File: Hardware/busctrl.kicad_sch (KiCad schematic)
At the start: 22 parts, among them J13 ICSP, J2 Conn_02x05_Odd_Even, J8 POWER, J8 RESET, J9 IDE, SW1 PWR, SW1 RST, U2 ATF1508AS, U3 CY23022, U30 ATmega328P-P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

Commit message: PCB cleanup
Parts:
- added C15: 1uF, Capacitor_SMD:C_0402_1005Metric_Pad0.74x0.62mm_HandSolder, symbol Device:C_Small
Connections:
- net +5V: no longer C28.1, C28.1, J13.2 (Pin_2), R6.1, U30.20 (AVCC), U30.7 (VCC)
- net GND: now also C15.2
- new net +5VP: C15.1, C28.1, C28.1, J13.2 (Pin_2), R6.1, U30.20 (AVCC), U30.7 (VCC)

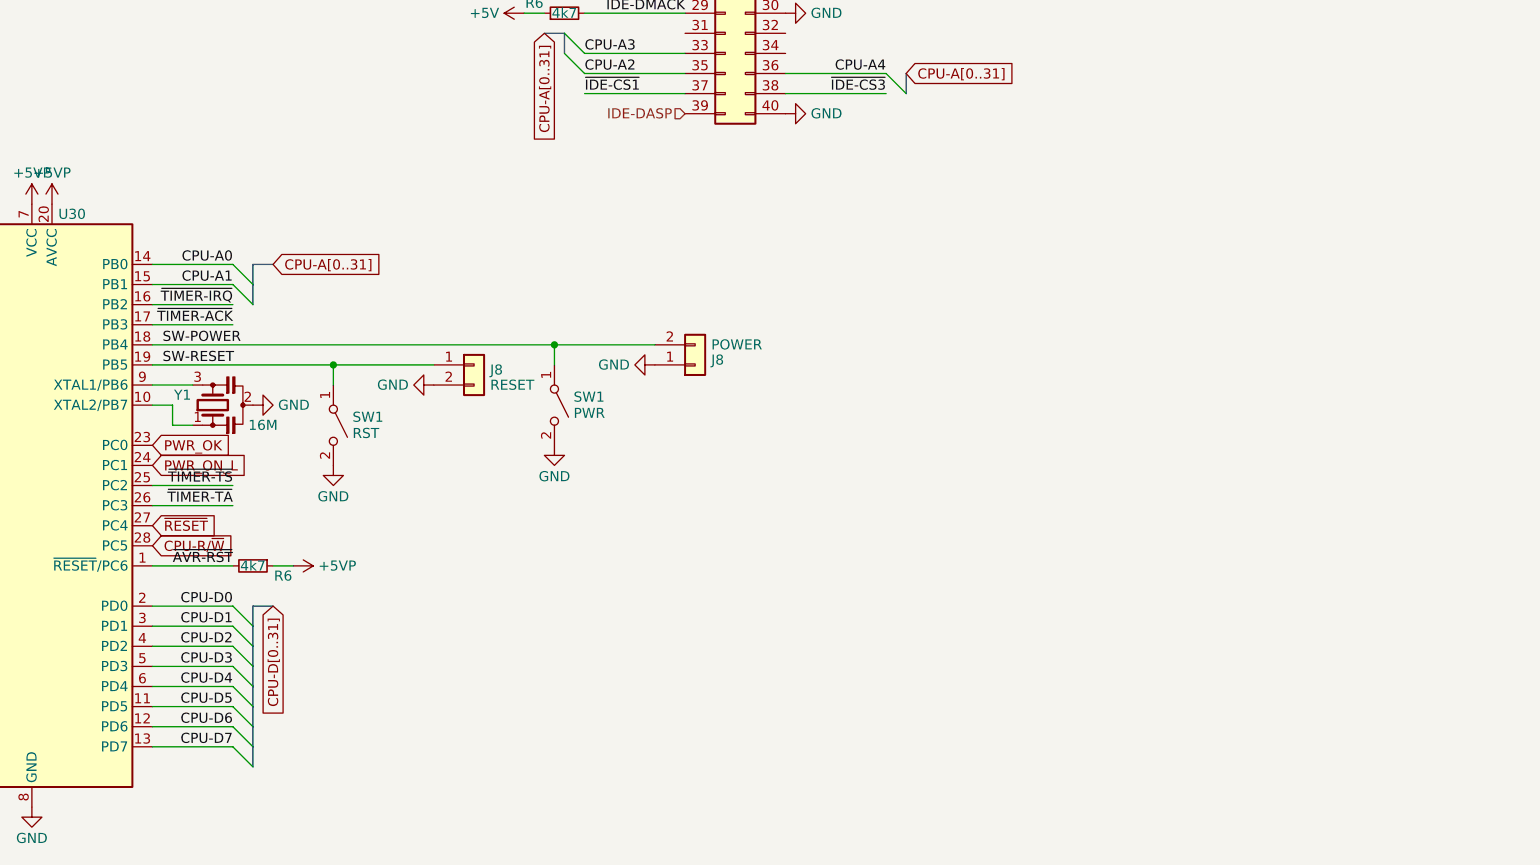
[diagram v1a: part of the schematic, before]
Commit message: Add data bus buffer to timer
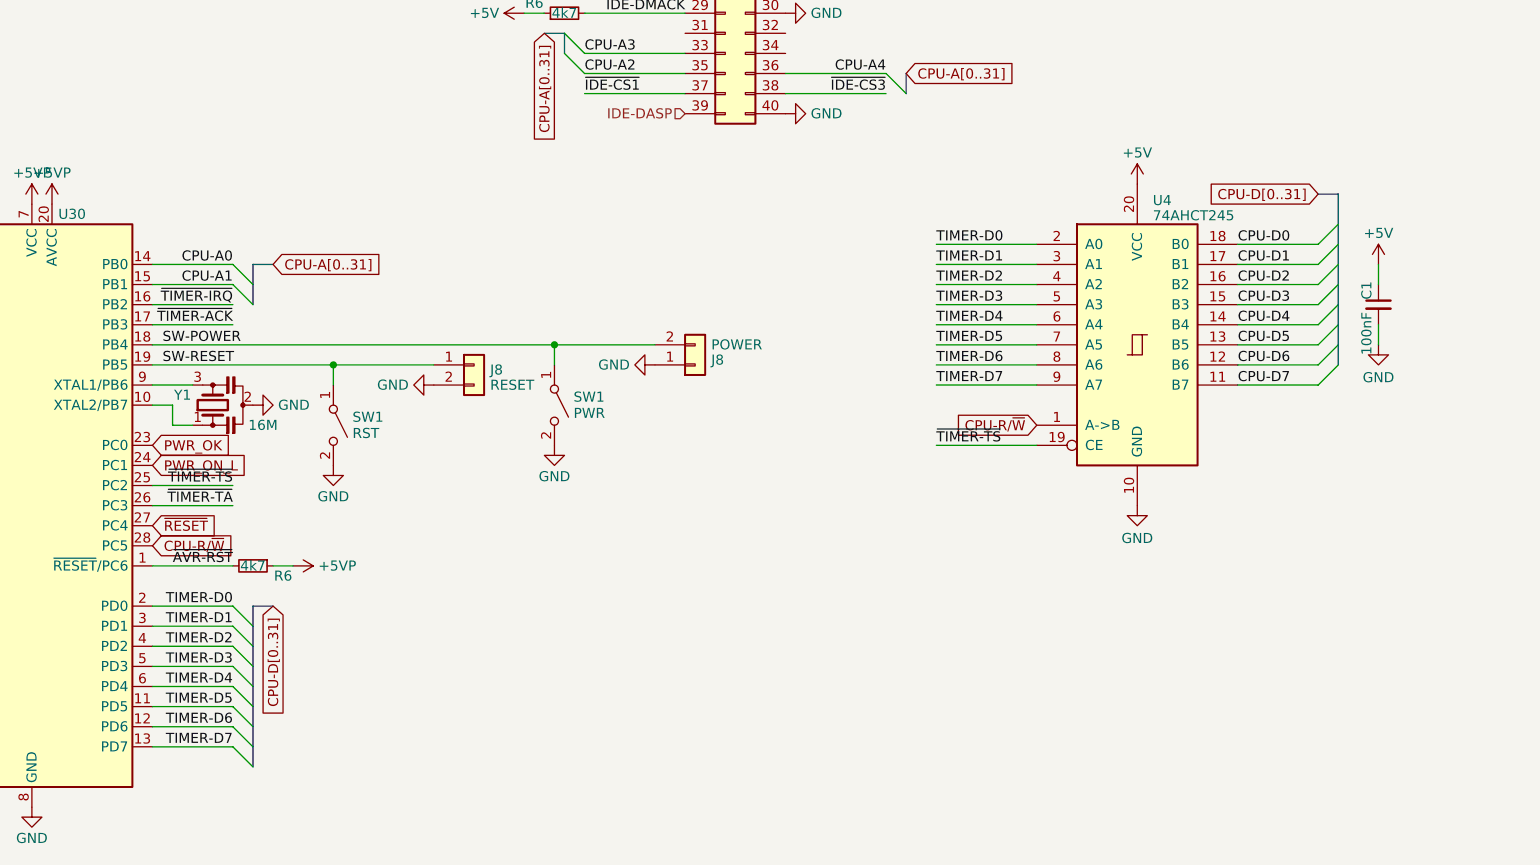
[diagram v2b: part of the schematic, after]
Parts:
- added C1: 100nF, Capacitor_SMD:C_0402_1005Metric_Pad0.74x0.62mm_HandSolder, symbol Device:C_Small
- added U4: 74AHCT245, Package_SO:SSOP-20_5.3x7.2mm_P0.65mm, symbol 74xx:74HC245
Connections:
- net +5V: now also C1.1, U4.20 (VCC)
- net CPU-D0: now also U4.18 (B0); no longer U30.2 (PD0)
- net CPU-D1: now also U4.17 (B1); no longer U30.3 (PD1)
- net CPU-D2: now also U4.16 (B2); no longer U30.4 (PD2)
- net CPU-D3: now also U4.15 (B3); no longer U30.5 (PD3)
- net CPU-D4: now also U4.14 (B4); no longer U30.6 (PD4)
- net CPU-D5: now also U4.13 (B5); no longer U30.11 (PD5)
- net CPU-D6: now also U4.12 (B6); no longer U30.12 (PD6)
- net CPU-D7: now also U4.11 (B7); no longer U30.13 (PD7)
- net CPU-R/~{W}: now also U4.1 (A->B)
- net GND: now also C1.2, U4.10 (GND)
- net ~{TIMER-TS}: now also U4.19 (CE)
- new net TIMER-D0: U30.2 (PD0), U4.2 (A0)
- new net TIMER-D1: U30.3 (PD1), U4.3 (A1)
- new net TIMER-D2: U30.4 (PD2), U4.4 (A2)
- new net TIMER-D3: U30.5 (PD3), U4.5 (A3)
- new net TIMER-D4: U30.6 (PD4), U4.6 (A4)
- new net TIMER-D5: U30.11 (PD5), U4.7 (A5)
- new net TIMER-D6: U30.12 (PD6), U4.8 (A6)
- new net TIMER-D7: U30.13 (PD7), U4.9 (A7)

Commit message: DRC cleanup
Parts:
- removed J8: RESET, Connector_PinHeader_2.54mm:PinHeader_1x02_P2.54mm_Vertical, symbol Connector_Generic:Conn_01x02
- removed J8: POWER, Connector_PinHeader_2.54mm:PinHeader_1x02_P2.54mm_Vertical, symbol Connector_Generic:Conn_01x02
- added J14: Conn_02x04_Odd_Even, Connector_PinHeader_2.54mm:PinHeader_2x04_P2.54mm_Vertical, symbol Connector_Generic:Conn_02x04_Odd_Even
- added R10, R56: 1k, Resistor_SMD:R_0402_1005Metric, symbol Device:R_Small
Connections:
- net +5V: now also R56.1
- net GND: now also J14.1 (Pin_1), J14.4 (Pin_4), J14.5 (Pin_5), J14.8 (Pin_8)
- net IDE-DASP: now also R10.1
- net SW-POWER: now also J14.3 (Pin_3)
- net SW-RESET: now also J14.2 (Pin_2)
- new net HDD-LED: J14.6 (Pin_6), R10.2
- new net PWR-LED: J14.7 (Pin_7), R56.2
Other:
- moved on the sheet: SW1
